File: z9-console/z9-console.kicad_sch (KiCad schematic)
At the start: 4 parts

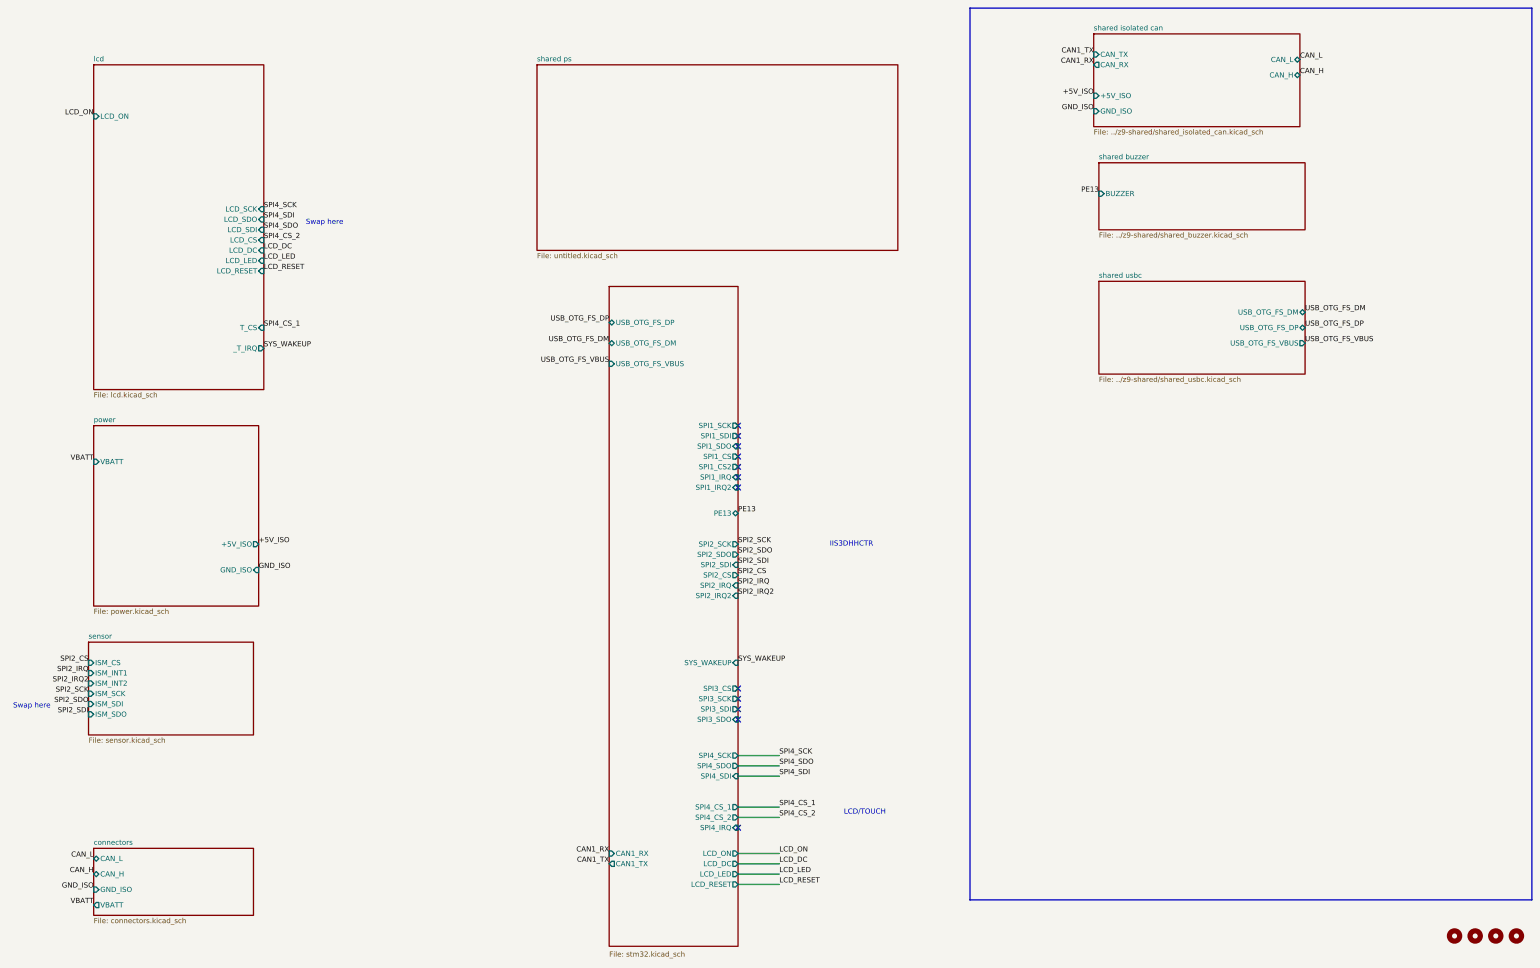
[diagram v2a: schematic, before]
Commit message: Update schematic and project configuration
- Changed the starting number for annotation in the project configuration from 300 to 700.
- Removed the "+5V_ISO" label from the schematic.
- Adjusted the position of the "PE13" label.
- Added a new "VBATT" label in the schematic.
- Updated the "shared buzzer" sheet reference, changing its UUID and properties.
- Modified the pin configuration for the "BUZZER" input in the schematic.
- Cleaned up unused labels and adjusted pin placements for clarity.
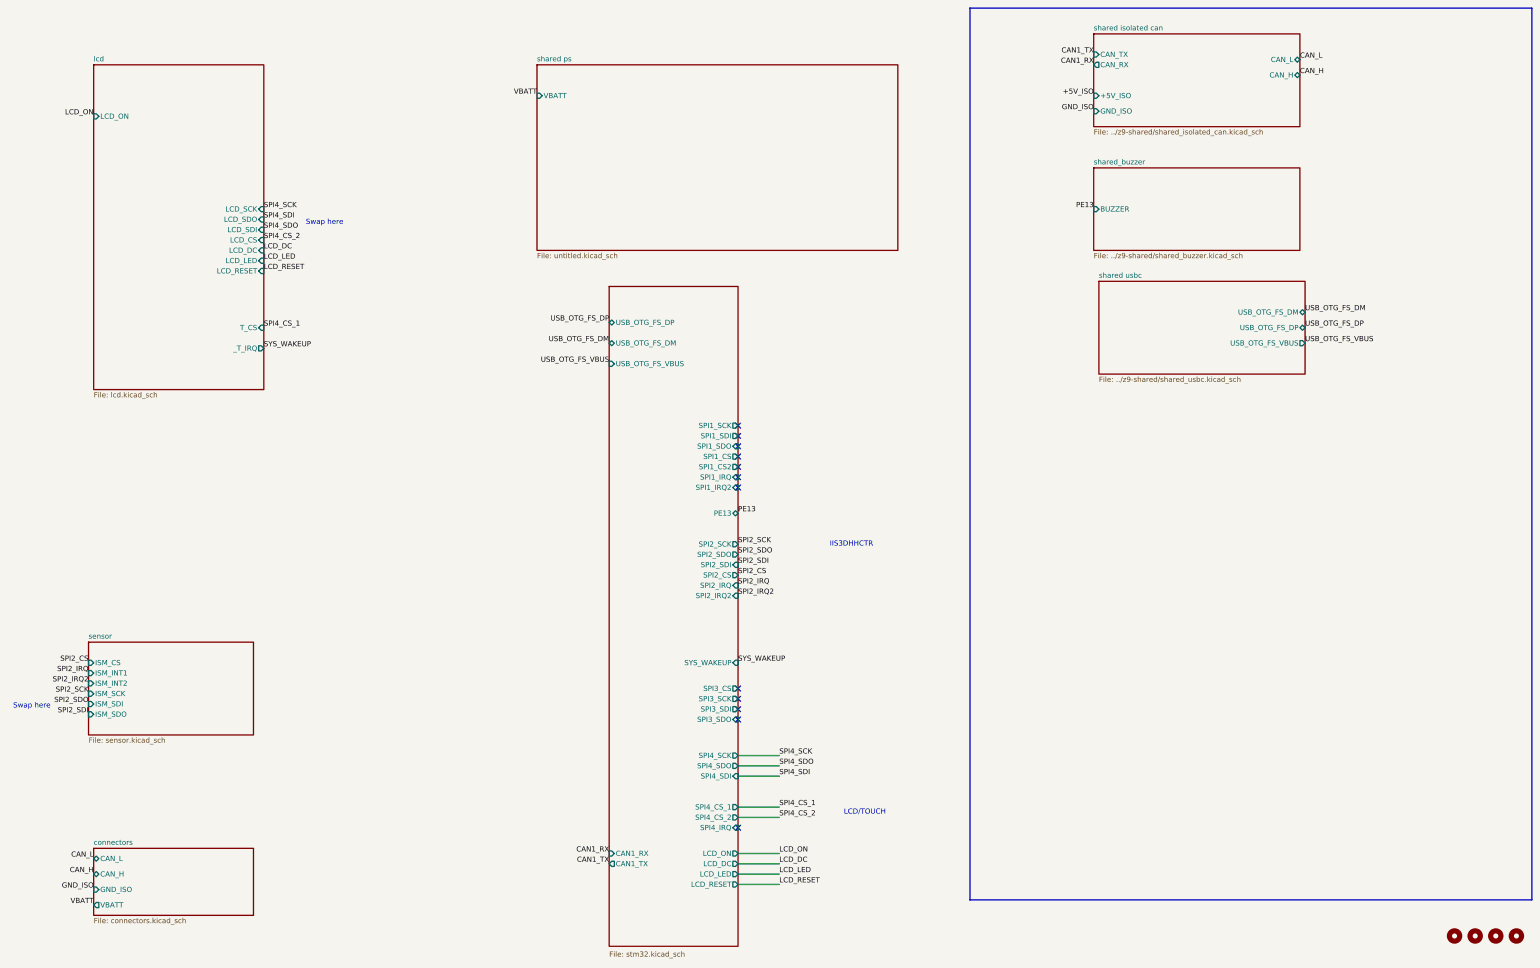
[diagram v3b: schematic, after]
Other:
- removed sheet power
- removed sheet shared buzzer
- added sheet shared_buzzer (../z9-shared/shared_buzzer.kicad_sch)
- sheet shared ps ports: added VBATT; removed none
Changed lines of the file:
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@@
-		)
-	)
-	(label "+5V_ISO"
-		(at 93.98 148.59 0)
-		(effects
-			(font
-				(size 1.27 1.27)
-			)
-			(justify left bottom)
 		)
 	)
@@
 	)
 	(label "PE13"
-		(at 300.99 62.23 180)
+		(at 299.72 66.04 180)
 		(effects
 			(font
@@
 		)
 	)
-	(label "GND_ISO"
-		(at 93.98 154.94 0)
-		(effects
-			(font
-				(size 1.27 1.27)
-			)
-			(justify left bottom)
-		)
-	)
 	(label "USB_OTG_FS_VBUS"
 		(at 180.34 104.14 180)
@@
 		)
 	)
+	(label "VBATT"
+		(at 162.56 38.1 180)
+		(effects
+			(font
+				(size 1.27 1.27)
+			)
+			(justify right bottom)
+		)
+	)
 	(label "SPI4_SCK"
 		(at 222.25 200.66 0)
@@
 	(label "+5V_ISO"
 		(at 299.72 38.1 180)
-		(effects
-			(font
-				(size 1.27 1.27)
-			)
-			(justify right bottom)
-		)
-	)
-	(label "VBATT"
-		(at 53.34 128.27 180)
 		(effects
 			(font
@@
 			)
 		)
+		(pin "VBATT" input
+			(at 162.56 38.1 180)
+			(effects
+				(font
+					(size 1.27 1.27)
+				)
+				(justify left)
+			)
+		)
 		(instances
 			(project "z9-console"
 				(path "/8d063f79-9282-4820-bcf4-1ff3c006cf08"
 					(page "10")
-				)
-			)
-		)
-	)
-	(sheet
-		(at 300.99 54.61)
-		(size 50.8 16.51)
-		(exclude_from_sim no)
-		(in_bom yes)
-		(on_board yes)
-		(dnp no)
-		(fields_autoplaced yes)
-		(stroke
-			(width 0.1524)
-			(type solid)
-		)
-		(fill
-			(color 0 0 0 0.0000)
-		)
-		(property "Sheetname" "shared buzzer"
-			(at 300.99 53.8984 0)
-			(effects
-				(font
-					(size 1.27 1.27)
-				)
-				(justify left bottom)
-			)
-		)
-		(property "Sheetfile" "../z9-shared/shared_buzzer.kicad_sch"
-			(at 300.99 71.7046 0)
-			(effects
-				(font
-					(size 1.27 1.27)
-				)
-				(justify left top)
-			)
-		)
-		(pin "BUZZER" input
-			(at 300.99 62.23 180)
-			(effects
-				(font
-					(size 1.27 1.27)
-				)
-				(justify left)
-			)
-		)
-		(instances
-			(project "z9-console"
-				(path "/8d063f79-9282-4820-bcf4-1ff3c006cf08"
-					(page "700")
 				)
 			)
@@
 	)
 	(sheet
-		(at 53.34 119.38)
-		(size 40.64 44.45)
+		(at 299.72 55.88)
+		(size 50.8 20.32)
 		(exclude_from_sim no)
 		(in_bom yes)
@@
 			(color 0 0 0 0.0000)
 		)
-		(property "Sheetname" "power"
-			(at 53.34 118.6684 0)
+		(property "Sheetname" "shared_buzzer"
+			(at 299.72 55.1684 0)
 			(effects
 				(font
@@
 			)
 		)
-		(property "Sheetfile" "power.kicad_sch"
-			(at 53.34 164.4146 0)
+		(property "Sheetfile" "../z9-shared/shared_buzzer.kicad_sch"
+			(at 299.72 76.7846 0)
 			(effects
 				(font
@@
 			)
 		)
-		(pin "GND_ISO" input
-			(at 93.98 154.94 0)
-			(effects
-				(font
-					(size 1.27 1.27)
-				)
-				(justify right)
-			)
-		)
-		(pin "+5V_ISO" output
-			(at 93.98 148.59 0)
-			(effects
-				(font
-					(size 1.27 1.27)
-				)
-				(justify right)
-			)
-		)
-		(pin "VBATT" input
-			(at 53.34 128.27 180)
+		(pin "BUZZER" input
+			(at 299.72 66.04 180)
 			(effects
 				(font
@@
 			(project "z9-console"
 				(path "/8d063f79-9282-4820-bcf4-1ff3c006cf08"
-					(page "5")
-				)
-			)
+					(page "11")
+				)
+			)
